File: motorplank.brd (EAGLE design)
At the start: 80 x 49 mm, 14 parts, among them IC1 74AHC1G86DBV

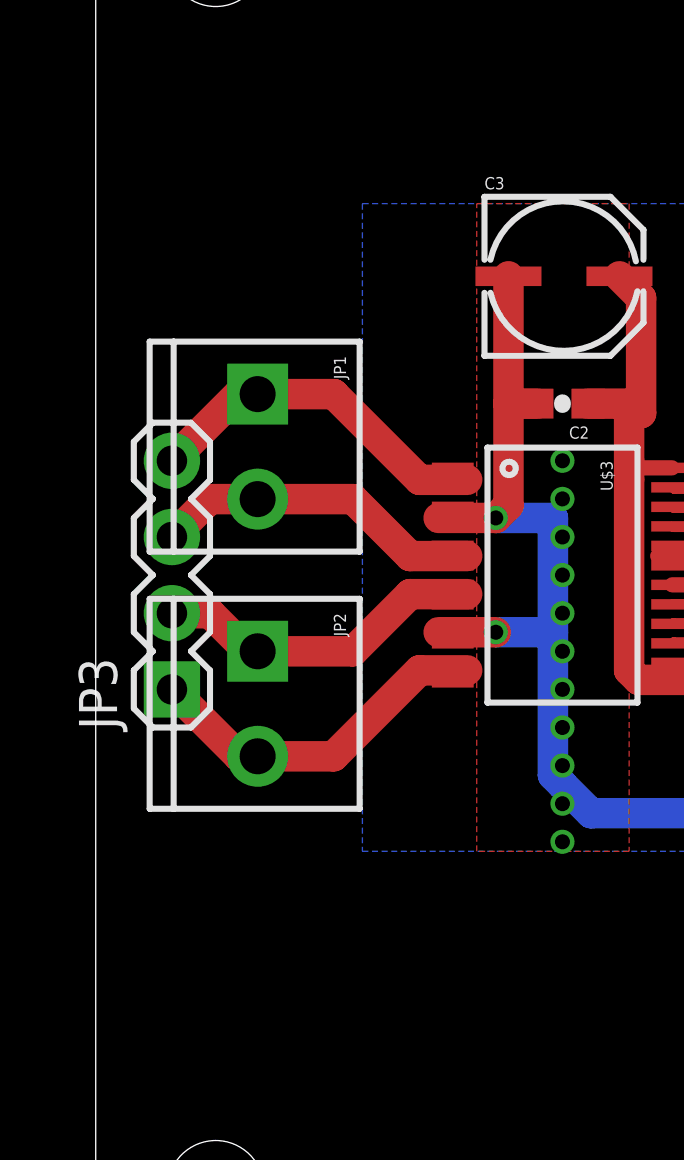
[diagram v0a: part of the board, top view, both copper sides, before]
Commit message: Add LED indicators for motor outputs.
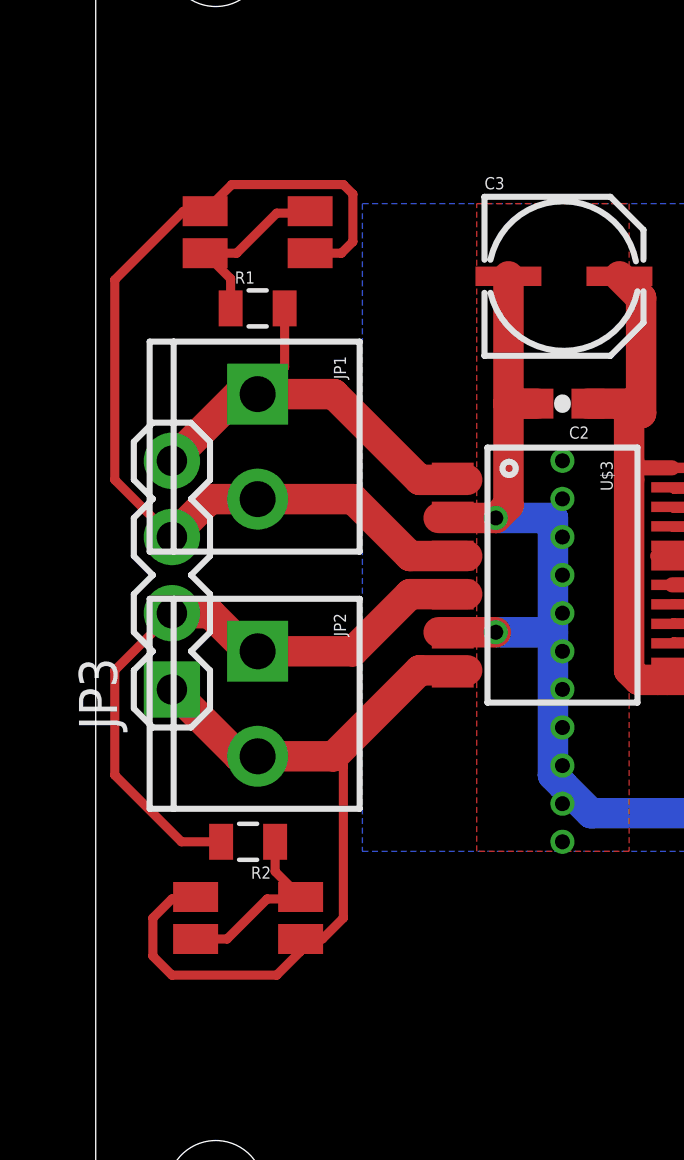
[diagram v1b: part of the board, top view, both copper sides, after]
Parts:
- added R1, R2: (no value), SparkFun-Passives:0805
- added U$5, U$6: BILED, nickparts:BILED
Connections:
- removed net N$28: JP2.2, JP3.1, U$3.11, U$3.12
- removed net N$30: JP1.2, JP3.3, U$3.5, U$3.6
- new net N$33: R1.1, U$5.A2, U$5.C1
- new net N$34: R2.1, U$6.A2, U$6.C1
- new net N$35: JP1.2, JP3.3, U$3.5, U$3.6, U$5.A1, U$5.C2
- new net N$36: JP2.2, JP3.1, U$3.11, U$3.12, U$6.A1, U$6.C2
- net N$27: now also R2.2
- net N$29: now also R1.2
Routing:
- net N$35: track 0.00 -> 34.2 mm
- net N$36: track 0.00 -> 29.3 mm
- net N$28: track 13.1 -> 0.00 mm
- net N$30: track 12.3 -> 0.00 mm
- net N$27: track 12.3 -> 23.0 mm
- net N$33: track 0.00 -> 6.27 mm
- net N$34: track 0.00 -> 6.27 mm
- net N$29: track 13.2 -> 16.5 mm
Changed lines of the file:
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@@
 <element name="C3" library="SparkFun-Passives" package="PANASONIC_C" value="10u" x="16.8275" y="34.6075"/>
 <element name="U$4" library="SparkFun-Aesthetics" package="OSHW-LOGO-M" value="" x="41.275" y="4.445"/>
+<element name="U$5" library="nickparts" package="BILED" value="BILED" x="6.6675" y="35.8775"/>
+<element name="U$6" library="nickparts" package="BILED" value="BILED" x="6.35" y="13.0175"/>
+<element name="R1" library="SparkFun-Passives" package="0805" value="" x="6.6675" y="33.3375"/>
+<element name="R2" library="SparkFun-Passives" package="0805" value="" x="6.35" y="15.5575" rot="R180"/>
 </elements>
 <signals>
@@
 <wire x1="13.1715" y1="24.1225" x2="13.6525" y2="23.8125" width="0.3048" layer="1"/>
 <wire x1="13.6525" y1="23.8125" x2="13.1715" y2="23.4725" width="0.3048" layer="1"/>
-</signal>
-<signal name="N$28">
-<contactref element="U$3" pad="11"/>
-<contactref element="JP2" pad="2"/>
-<contactref element="U$3" pad="12"/>
-<contactref element="JP3" pad="1"/>
-<wire x1="6.6675" y1="18.4075" x2="9.2" y2="18.4075" width="1.016" layer="1"/>
-<wire x1="9.2" y1="18.4075" x2="12.065" y2="21.2725" width="1.016" layer="1"/>
-<wire x1="12.065" y1="21.2725" x2="13.6525" y2="21.2725" width="1.016" layer="1"/>
-<wire x1="6.6675" y1="18.4075" x2="6.04" y2="18.4075" width="1.016" layer="1"/>
-<wire x1="6.04" y1="18.4075" x2="3.81" y2="20.6375" width="1.016" layer="1"/>
-<wire x1="13.1715" y1="21.5225" x2="13.6525" y2="21.2725" width="0.3048" layer="1"/>
-<wire x1="13.6525" y1="21.2725" x2="13.1715" y2="20.8725" width="0.3048" layer="1"/>
+<contactref element="R2" pad="2"/>
+<wire x1="5.45" y1="15.5575" x2="4.1275" y2="15.5575" width="0.3048" layer="1"/>
+<wire x1="4.1275" y1="15.5575" x2="1.905" y2="17.78" width="0.3048" layer="1"/>
+<wire x1="1.905" y1="17.78" x2="1.905" y2="21.2725" width="0.3048" layer="1"/>
+<wire x1="1.905" y1="21.2725" x2="3.81" y2="23.1775" width="0.3048" layer="1"/>
 </signal>
 <signal name="N$29">
@@
 <wire x1="13.1715" y1="28.0225" x2="13.1715" y2="27.3725" width="0.3048" layer="1"/>
 <wire x1="13.6525" y1="27.6225" x2="13.1715" y2="28.0225" width="0.3048" layer="1"/>
-</signal>
-<signal name="N$30">
-<contactref element="U$3" pad="5"/>
-<contactref element="JP1" pad="2"/>
-<contactref element="U$3" pad="6"/>
-<contactref element="JP3" pad="3"/>
-<wire x1="6.6675" y1="26.98" x2="9.85" y2="26.98" width="1.016" layer="1"/>
-<wire x1="9.85" y1="26.98" x2="11.7475" y2="25.0825" width="1.016" layer="1"/>
-<wire x1="11.7475" y1="25.0825" x2="13.6525" y2="25.0825" width="1.016" layer="1"/>
-<wire x1="6.6675" y1="26.98" x2="5.0725" y2="26.98" width="1.016" layer="1"/>
-<wire x1="5.0725" y1="26.98" x2="3.81" y2="25.7175" width="1.016" layer="1"/>
-<wire x1="13.1715" y1="25.4225" x2="13.6525" y2="25.0825" width="0.3048" layer="1"/>
-<wire x1="13.6525" y1="25.0825" x2="13.1715" y2="24.7725" width="0.3048" layer="1"/>
+<contactref element="R1" pad="2"/>
+<wire x1="7.5675" y1="33.3375" x2="7.5675" y2="31.38" width="0.3048" layer="1"/>
+<wire x1="7.5675" y1="31.38" x2="6.6675" y2="30.48" width="0.3048" layer="1"/>
 </signal>
 <signal name="VMOT">
@@
 <wire x1="20.536" y1="22.225" x2="20.4835" y2="22.1725" width="0.3048" layer="1"/>
 </signal>
+<signal name="N$33">
+<contactref element="U$5" pad="C1"/>
+<contactref element="R1" pad="1"/>
+<contactref element="U$5" pad="A2"/>
+<wire x1="5.7675" y1="33.3375" x2="5.7675" y2="34.3275" width="0.3048" layer="1"/>
+<wire x1="5.7675" y1="34.3275" x2="4.9175" y2="35.1775" width="0.3048" layer="1"/>
+<wire x1="4.9175" y1="35.1775" x2="5.9675" y2="35.1775" width="0.3048" layer="1"/>
+<wire x1="5.9675" y1="35.1775" x2="7.3025" y2="36.5125" width="0.3048" layer="1"/>
+<wire x1="7.3025" y1="36.5125" x2="8.3525" y2="36.5125" width="0.3048" layer="1"/>
+<wire x1="8.3525" y1="36.5125" x2="8.4175" y2="36.5775" width="0.3048" layer="1"/>
+</signal>
+<signal name="N$34">
+<contactref element="U$6" pad="C1"/>
+<contactref element="R2" pad="1"/>
+<contactref element="U$6" pad="A2"/>
+<wire x1="7.25" y1="15.5575" x2="7.25" y2="14.5675" width="0.3048" layer="1"/>
+<wire x1="7.25" y1="14.5675" x2="8.1" y2="13.7175" width="0.3048" layer="1"/>
+<wire x1="4.6" y1="12.3175" x2="5.65" y2="12.3175" width="0.3048" layer="1"/>
+<wire x1="5.65" y1="12.3175" x2="6.985" y2="13.6525" width="0.3048" layer="1"/>
+<wire x1="6.985" y1="13.6525" x2="8.035" y2="13.6525" width="0.3048" layer="1"/>
+<wire x1="8.035" y1="13.6525" x2="8.1" y2="13.7175" width="0.3048" layer="1"/>
+</signal>
+<signal name="N$35">
+<contactref element="U$5" pad="A1"/>
+<contactref element="U$5" pad="C2"/>
+<contactref element="U$3" pad="5"/>
+<contactref element="JP1" pad="2"/>
+<contactref element="U$3" pad="6"/>
+<contactref element="JP3" pad="3"/>
+<wire x1="6.6675" y1="26.98" x2="9.85" y2="26.98" width="1.016" layer="1"/>
+<wire x1="9.85" y1="26.98" x2="11.7475" y2="25.0825" width="1.016" layer="1"/>
+<wire x1="11.7475" y1="25.0825" x2="13.6525" y2="25.0825" width="1.016" layer="1"/>
+<wire x1="6.6675" y1="26.98" x2="5.0725" y2="26.98" width="1.016" layer="1"/>
+<wire x1="5.0725" y1="26.98" x2="3.81" y2="25.7175" width="1.016" layer="1"/>
+<wire x1="13.1715" y1="25.4225" x2="13.6525" y2="25.0825" width="0.3048" layer="1"/>
+<wire x1="13.6525" y1="25.0825" x2="13.1715" y2="24.7725" width="0.3048" layer="1"/>
+<wire x1="4.9175" y1="36.5775" x2="4.1925" y2="36.5775" width="0.3048" layer="1"/>
+<wire x1="4.1925" y1="36.5775" x2="1.905" y2="34.29" width="0.3048" layer="1"/>
+<wire x1="1.905" y1="34.29" x2="1.905" y2="27.6225" width="0.3048" layer="1"/>
+<wire x1="1.905" y1="27.6225" x2="3.81" y2="25.7175" width="0.3048" layer="1"/>
+<wire x1="8.4175" y1="35.1775" x2="9.46" y2="35.1775" width="0.3048" layer="1"/>
+<wire x1="9.46" y1="35.1775" x2="9.8425" y2="35.56" width="0.3048" layer="1"/>
+<wire x1="9.8425" y1="35.56" x2="9.8425" y2="37.1475" width="0.3048" layer="1"/>
+<wire x1="9.8425" y1="37.1475" x2="9.525" y2="37.465" width="0.3048" layer="1"/>
+<wire x1="9.525" y1="37.465" x2="5.805" y2="37.465" width="0.3048" layer="1"/>
+<wire x1="5.805" y1="37.465" x2="4.9175" y2="36.5775" width="0.3048" layer="1"/>
+</signal>
+<signal name="N$36">
+<contactref element="U$6" pad="A1"/>
+<contactref element="U$6" pad="C2"/>
+<contactref element="U$3" pad="11"/>
+<contactref element="JP2" pad="2"/>
+<contactref element="U$3" pad="12"/>
+<contactref element="JP3" pad="1"/>
+<wire x1="6.6675" y1="18.4075" x2="9.2" y2="18.4075" width="1.016" layer="1"/>
+<wire x1="9.2" y1="18.4075" x2="12.065" y2="21.2725" width="1.016" layer="1"/>
+<wire x1="12.065" y1="21.2725" x2="13.6525" y2="21.2725" width="1.016" layer="1"/>
+<wire x1="6.6675" y1="18.4075" x2="6.04" y2="18.4075" width="1.016" layer="1"/>
+<wire x1="6.04" y1="18.4075" x2="3.81" y2="20.6375" width="1.016" layer="1"/>
+<wire x1="13.1715" y1="21.5225" x2="13.6525" y2="21.2725" width="0.3048" layer="1"/>
+<wire x1="13.6525" y1="21.2725" x2="13.1715" y2="20.8725" width="0.3048" layer="1"/>
+<wire x1="8.1" y1="12.3175" x2="8.1" y2="11.91" width="0.3048" layer="1"/>
+<wire x1="8.1" y1="11.91" x2="7.3025" y2="11.1125" width="0.3048" layer="1"/>
+<wire x1="7.3025" y1="11.1125" x2="3.81" y2="11.1125" width="0.3048" layer="1"/>
+<wire x1="3.81" y1="11.1125" x2="3.175" y2="11.7475" width="0.3048" layer="1"/>
+<wire x1="3.175" y1="11.7475" x2="3.175" y2="13.0175" width="0.3048" layer="1"/>
+<wire x1="3.175" y1="13.0175" x2="3.81" y2="13.6525" width="0.3048" layer="1"/>
+<wire x1="3.81" y1="13.6525" x2="4.535" y2="13.6525" width="0.3048" layer="1"/>
+<wire x1="4.535" y1="13.6525" x2="4.6" y2="13.7175" width="0.3048" layer="1"/>
+<wire x1="8.1" y1="12.3175" x2="8.825" y2="12.3175" width="0.3048" layer="1"/>
+<wire x1="8.825" y1="12.3175" x2="9.525" y2="13.0175" width="0.3048" layer="1"/>
+<wire x1="9.525" y1="13.0175" x2="9.525" y2="18.0825" width="0.3048" layer="1"/>
+<wire x1="9.525" y1="18.0825" x2="9.2" y2="18.4075" width="0.3048" layer="1"/>
+</signal>
 </signals>
